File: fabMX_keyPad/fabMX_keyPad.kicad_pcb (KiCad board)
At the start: 2 copper layers, 60 x 165 mm, 114 parts, among them J1 USB_C_Receptacle_USB2.0, J2 Conn_02x03_Odd_Even, J3 Conn_01x04, J6 Conn_01x04, J7 Conn_01x12, SW10 SW_Push, SW11 SW_Push, SW12 SW_Push, SW20 SW_Push, SW21 SW_Push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

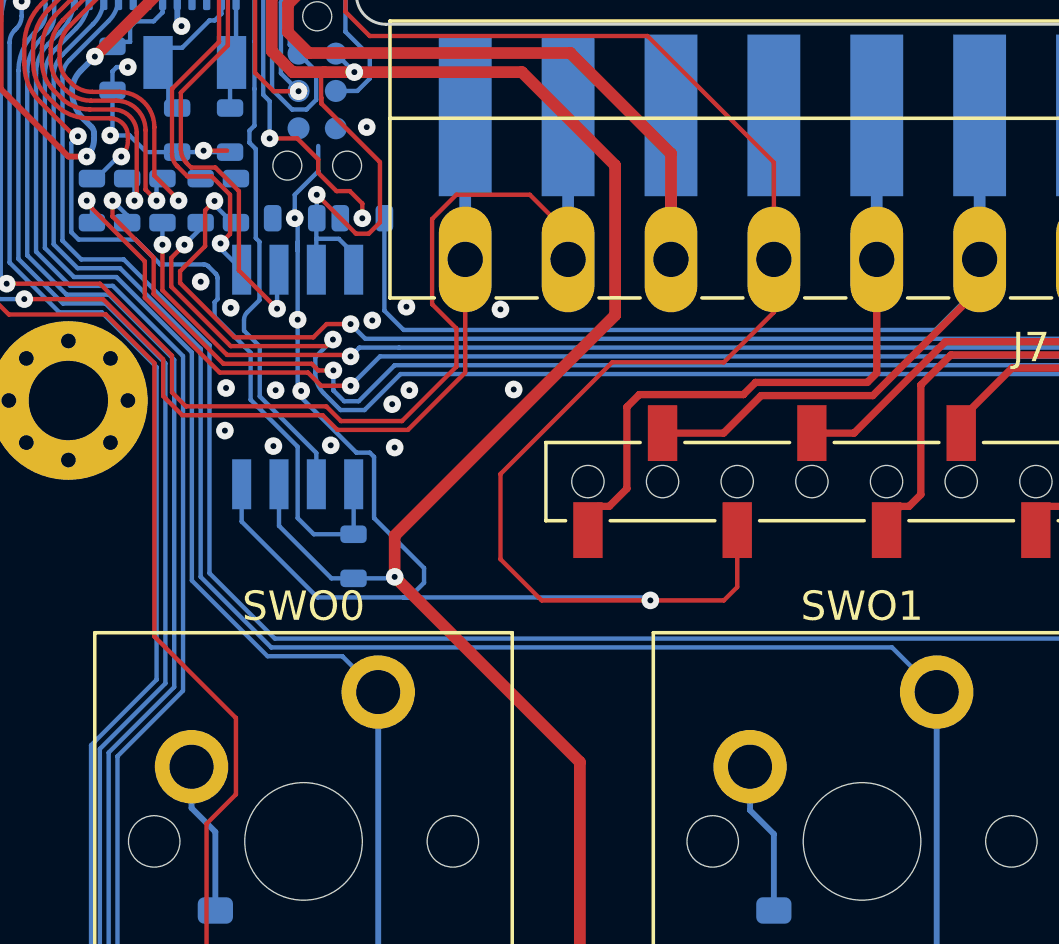
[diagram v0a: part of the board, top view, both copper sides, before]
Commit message: Fixes from @fkreiner 's feedback at 37C3
Connected NFC_CS' and NFC_RST' signals to MCU
Added additional Jumper-R to connect NFC_3V3 to global 3.3V net
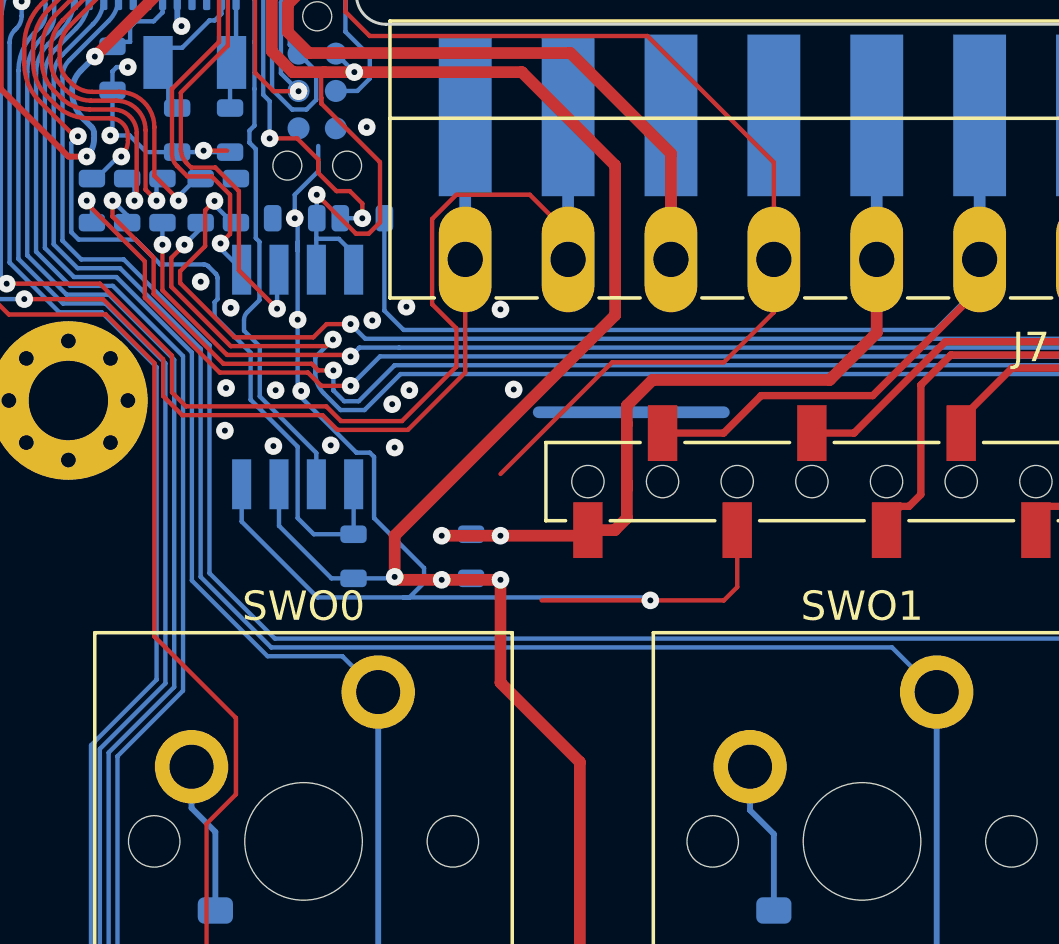
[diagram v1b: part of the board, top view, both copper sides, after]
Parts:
- added R18: 0, dipolMods:R_0603_min, B.Cu at (77.0, 97.1)
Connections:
- U1 pad 27: /D10 -> /NFC_CS'
- U1 pad 47: /A5 -> /NFC_RST'
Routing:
- net /NFC_CS': track 0.00 -> 24.7 mm, vias 0 -> 2
- net /D10: track 23.6 -> 0.00 mm, vias 2 -> 0
- net /NFC_3V3: track 23.0 -> 38.1 mm, vias 0 -> 2
- net /NFC_RST': track 0.00 -> 12.4 mm, vias 0 -> 2
- net /A5: track 11.7 -> 0.00 mm, vias 2 -> 0
- net GND: track 151.9 -> 147.0 mm
- net 3.3V: track 459.6 -> 463.6 mm, vias 27 -> 29

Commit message: DRC and minor fix
DRC okay
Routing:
- net /NFC_3V3: track 38.1 -> 31.8 mm
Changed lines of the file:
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@@
   (segment (start 90.75 82.1) (end 90.75 87) (width 0.4) (layer "B.Cu") (net 81))
   (segment (start 77 96.4) (end 77.95 96.4) (width 0.2) (layer "B.Cu") (net 81))
-  (segment (start 79.25 92.2) (end 85.55 92.2) (width 0.4) (layer "B.Cu") (net 81))
   (segment (start 91.551238 95.399444) (end 91.85 95.399444) (width 0.25) (layer "F.Cu") (net 82))
   (segment (start 72.8005 90.2505) (end 72.85 90.3) (width 0.15) (layer "F.Cu") (net 82))
